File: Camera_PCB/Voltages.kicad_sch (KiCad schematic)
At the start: 31 parts

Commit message: cleaned up PCB branch
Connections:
- net GNDREF renamed GND

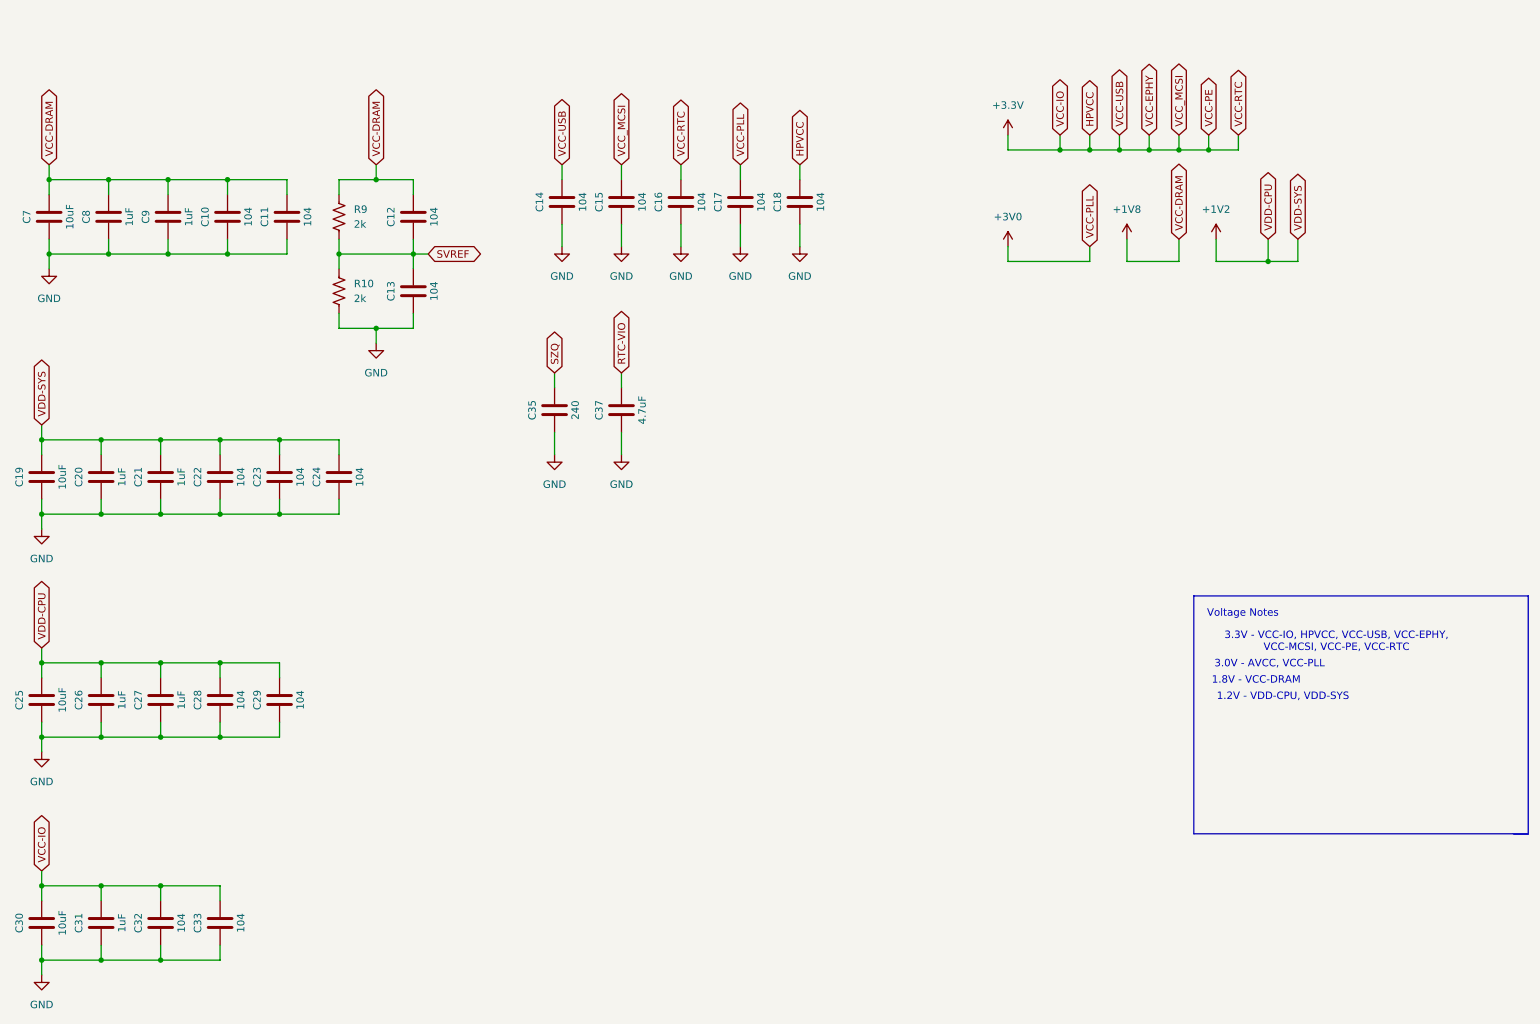
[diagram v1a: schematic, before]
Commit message: 10/29 Footprint Additions
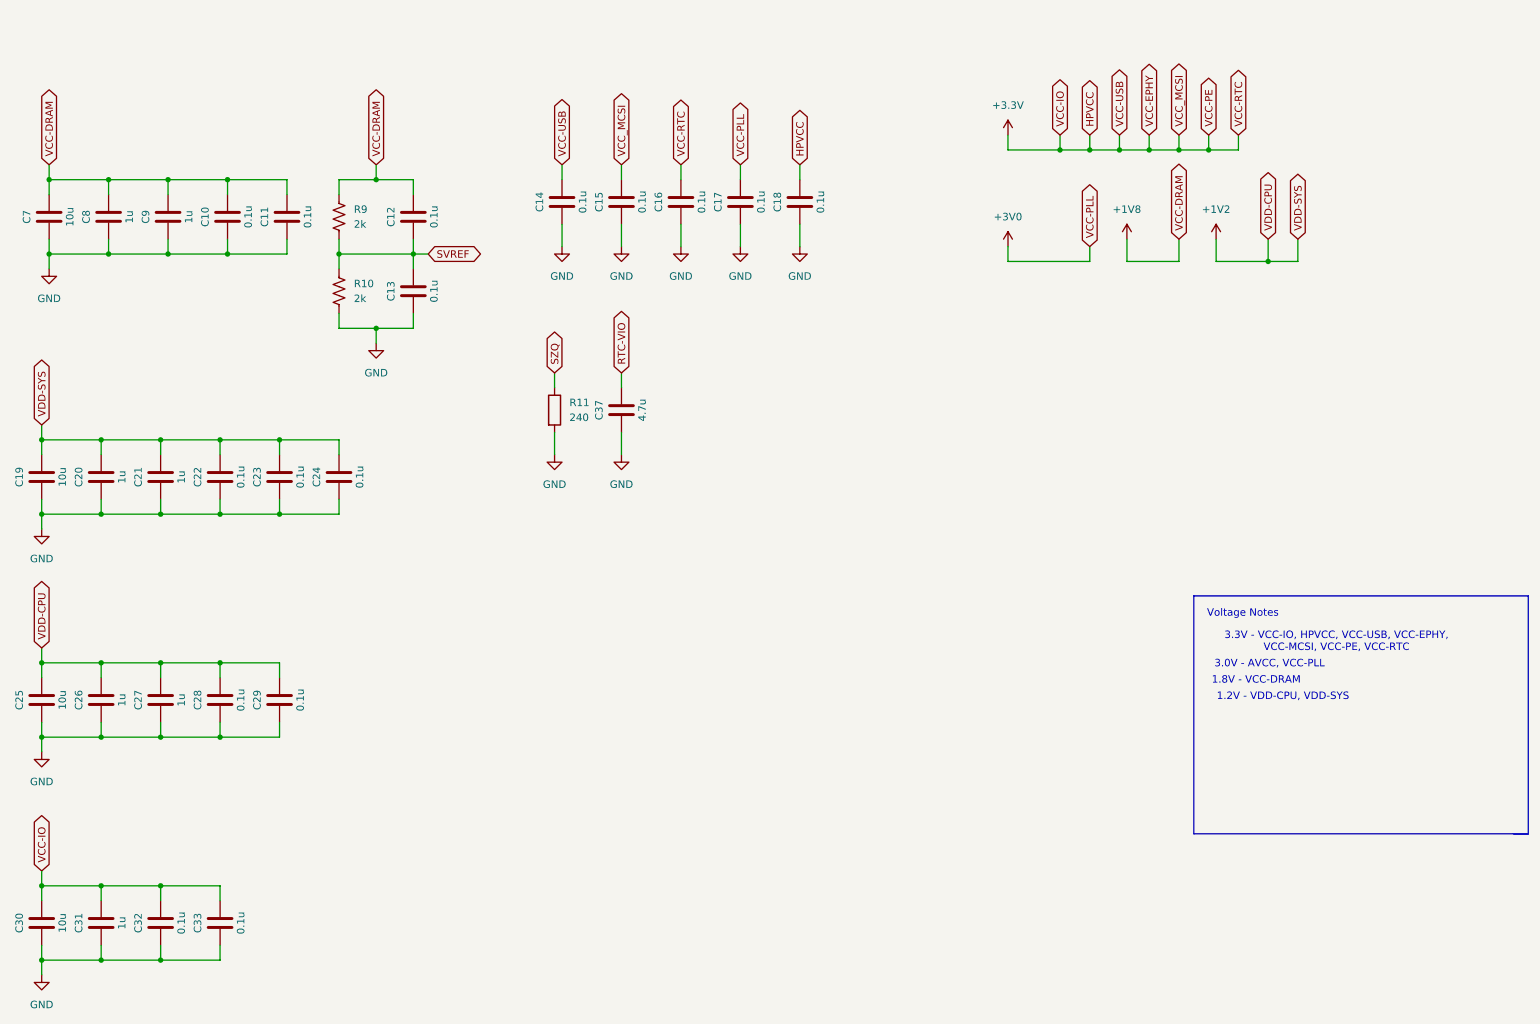
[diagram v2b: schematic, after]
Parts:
- removed C35: 240, Capacitor_SMD:C_0805_2012Metric_Pad1.18x1.45mm_HandSolder, symbol Device:C
- added R11: 240, symbol Device:R
- C10, C11, C12, C13, C14, C15, C16, C17, C18, C22, C23, C24, C28, C29, C32, C33: value 104 -> 0.1u; footprint Capacitor_SMD:C_0805_2012Metric_Pad1.18x1.45mm_HandSolder -> Capacitor_SMD:C_0603_1608Metric_Pad1.08x0.95mm_HandSolder
- C19, C25, C30, C7: value 10uF -> 10u
- C20, C21, C26, C27, C31, C8, C9: value 1uF -> 1u
- C37: value 4.7uF -> 4.7u
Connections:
- net GND: now also R11.2
- net SZQ: now also R11.1

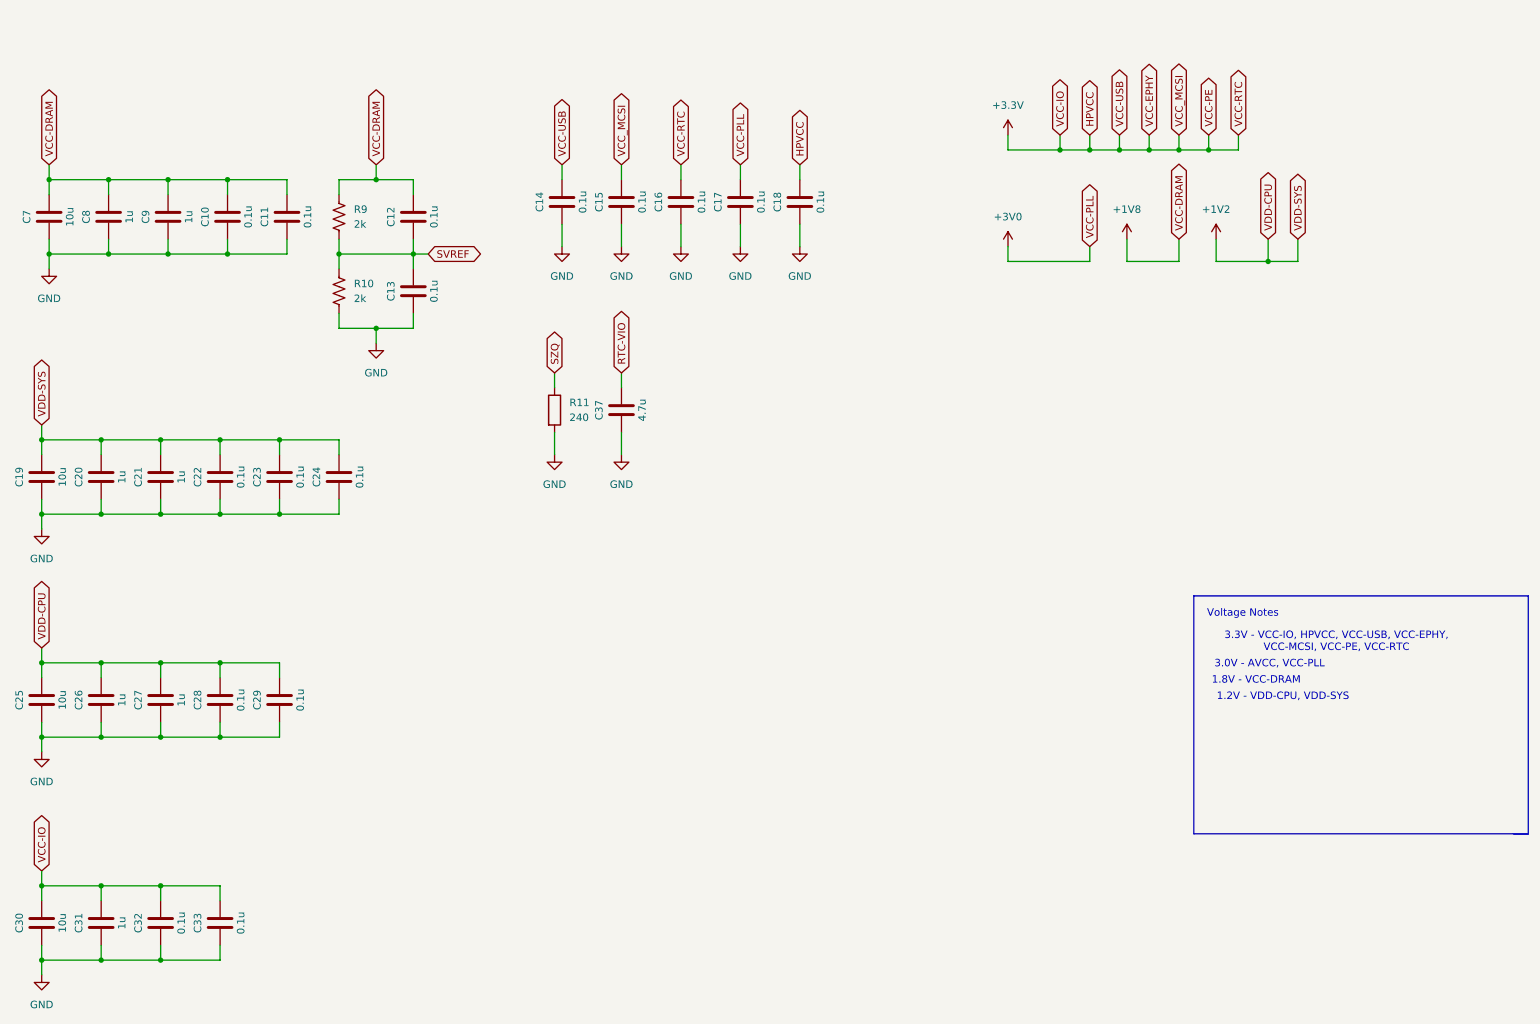
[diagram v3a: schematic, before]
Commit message: Schematic done, thoroughly reviewed by Jack, should get reviewed by Connor if possible.
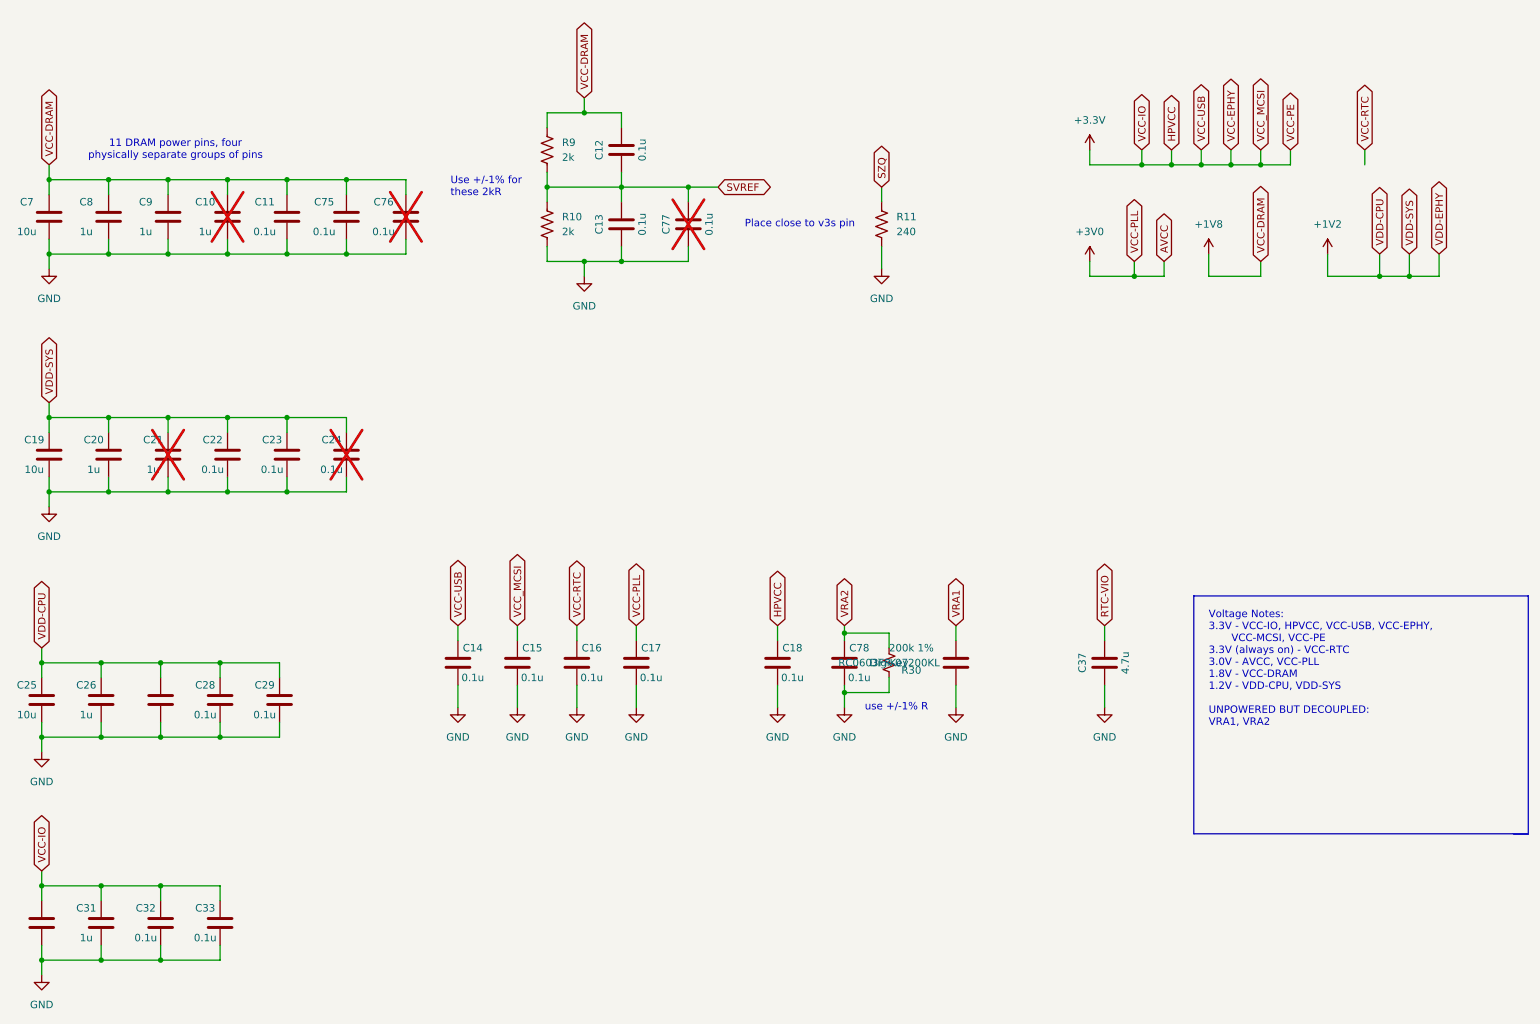
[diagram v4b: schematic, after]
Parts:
- removed R11: 240, symbol Device:R
- added C75, C76, C77, C78, C79: 0.1u, Capacitor_SMD:C_0603_1608Metric_Pad1.08x0.95mm_HandSolder, symbol Device:C
- added R11: 240, Resistor_SMD:R_0603_1608Metric_Pad0.98x0.95mm_HandSolder, symbol Device:R_US
- added R30: 200k 1%, Resistor_SMD:R_0603_1608Metric_Pad0.98x0.95mm_HandSolder, symbol Device:R_Small_US
- C10: value 0.1u -> 1u; DPN (none) -> GCM188R71E105KA64D; Distributor (none) -> DigiKey; now not fitted
- C11, C12, C13, C14, C15, C16, C17, C18, C22, C23, C28, C29, C32, C33: DPN (none) -> GRM188R72A104KA35D; Distributor (none) -> DigiKey
- C19, C25, C30, C7: DPN (none) -> GRM21BZ71E106KE15L; Distributor (none) -> DigiKey
- C20, C26, C27, C31, C8, C9: footprint Capacitor_SMD:C_0805_2012Metric_Pad1.18x1.45mm_HandSolder -> Capacitor_SMD:C_0603_1608Metric_Pad1.08x0.95mm_HandSolder; DPN (none) -> GCM188R71E105KA64D; Distributor (none) -> DigiKey
- C21: footprint Capacitor_SMD:C_0805_2012Metric_Pad1.18x1.45mm_HandSolder -> Capacitor_SMD:C_0603_1608Metric_Pad1.08x0.95mm_HandSolder; DPN (none) -> GCM188R71E105KA64D; Distributor (none) -> DigiKey; now not fitted
- C24: DPN (none) -> GRM188R72A104KA35D; Distributor (none) -> DigiKey; now not fitted
- C37: DPN (none) -> GRM21BZ71H475ME15K; Distributor (none) -> DigiKey
- R10, R9: footprint Resistor_SMD:R_0805_2012Metric_Pad1.20x1.40mm_HandSolder -> Resistor_SMD:R_0603_1608Metric_Pad0.98x0.95mm_HandSolder; DPN (none) -> RC0603FR-102KL; Distributor (none) -> DigiKey
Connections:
- net +1V8: now also C75.2, C76.2
- net +3.3V: no longer C16.2
- net GND: now also C75.1, C76.1, C77.1, C78.1, C79.1, R11.2, R30.1
- net SVREF: now also C77.2
- net SZQ: now also R11.1
- new net VCC-RTC: C16.2
- new net VRA1: C79.2
- new net VRA2: C78.2, R30.2
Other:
- note added: "11 DRAM power pins, four physically separate groups of pins"
- note added: "Place close to v3s pin"
- note added: "Use +/-1% for these 2kR"
- note added: "Voltage Notes: 3.3V - VCC-IO, HPVCC, VCC-USB, VCC-EPHY, VCC-MCSI, VCC-PE 3.3V (always on) - VCC-RTC 3.0V - AVCC, VCC-PLL 1.8V - VCC-DRAM 1.2V - VDD-CPU, VDD-SYS UNPOWERED BUT DECOUPLED: VRA1, VRA2"
- note added: "use +/-1% R"
- note removed: "1.2V - VDD-CPU, VDD-SYS"
- note removed: "1.8V - VCC-DRAM"
- note removed: "3.0V - AVCC, VCC-PLL"
- note removed: "3.3V - VCC-IO, HPVCC, VCC-USB, VCC-EPHY, VCC-MCSI, VCC-PE, VCC-RTC"
- note removed: "Voltage Notes"
- moved on the sheet: C12, C13, C14, C15, C16, C17, C18, C19, C20, C22, C23, C37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
